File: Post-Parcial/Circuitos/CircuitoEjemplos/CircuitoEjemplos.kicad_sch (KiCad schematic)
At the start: 7 parts

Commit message: Cambio de estructura
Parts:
- removed J? (x2): Conn_01x19, symbol Connector_Generic:Conn_01x19
- added D3, D4: LED, symbol Device:LED
- added J1, J2: Conn_01x19, Connector_PinSocket_2.54mm:PinSocket_1x19_P2.54mm_Vertical, symbol Connector_Generic:Conn_01x19
- added R3, R4: 330, symbol Device:R
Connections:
- net GPIO4: now reaches R2.1
- net GPIO4: now also J2.13 (Pin_13)
- net at R2.2: now also D2.2 (A)
- net GND: now reaches D2.1 (K)
- net GND: now also D1.1 (K), D3.1 (K), D4.1 (K), J1.14 (Pin_14), J2.1 (Pin_1), J2.7 (Pin_7)
- net GPIO2: now reaches R1.1
- net GPIO2: now also J2.15 (Pin_15)
- net at R1.2: now also D1.2 (A)
- new net: D4.2 (A), R4.2
- new net: D3.2 (A), R3.2
- new net 3.3V: J1.1 (Pin_1)
- new net 5V: J1.19 (Pin_19)
- new net GPI34: J1.5 (Pin_5)
- new net GPI35: J1.6 (Pin_6)
- new net GPI36: J1.3 (Pin_3)
- new net GPI39: J1.4 (Pin_4)
- new net GPIO0: J2.14 (Pin_14)
- new net GPIO12: J1.13 (Pin_13)
- new net GPIO13: J1.15 (Pin_15)
- new net GPIO14: J1.12 (Pin_12)
- new net GPIO15: J2.16 (Pin_16)
- new net GPIO16: J2.12 (Pin_12), R3.1
- new net GPIO17: J2.11 (Pin_11), R4.1
- new net GPIO18: J2.9 (Pin_9)
- new net GPIO19: J2.8 (Pin_8)
- new net GPIO21: J2.6 (Pin_6)
- new net GPIO22: J2.3 (Pin_3)
- new net GPIO23: J2.2 (Pin_2)
- new net GPIO25: J1.9 (Pin_9)
- new net GPIO26: J1.10 (Pin_10)
- new net GPIO27: J1.11 (Pin_11)
- new net GPIO32: J1.7 (Pin_7)
- new net GPIO33: J1.8 (Pin_8)
- new net GPIO5: J2.10 (Pin_10)
- new net RX/GPIO3: J2.5 (Pin_5)
- new net TX/GPIO1: J2.4 (Pin_4)
- no-connect marks 0 -> 7
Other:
- note added: "Conexión de Led's"
- note added: "ESP32_Devkitc_V4"
- note added: "USB en este sentido"
- moved on the sheet: D1, R1, R2, RV1

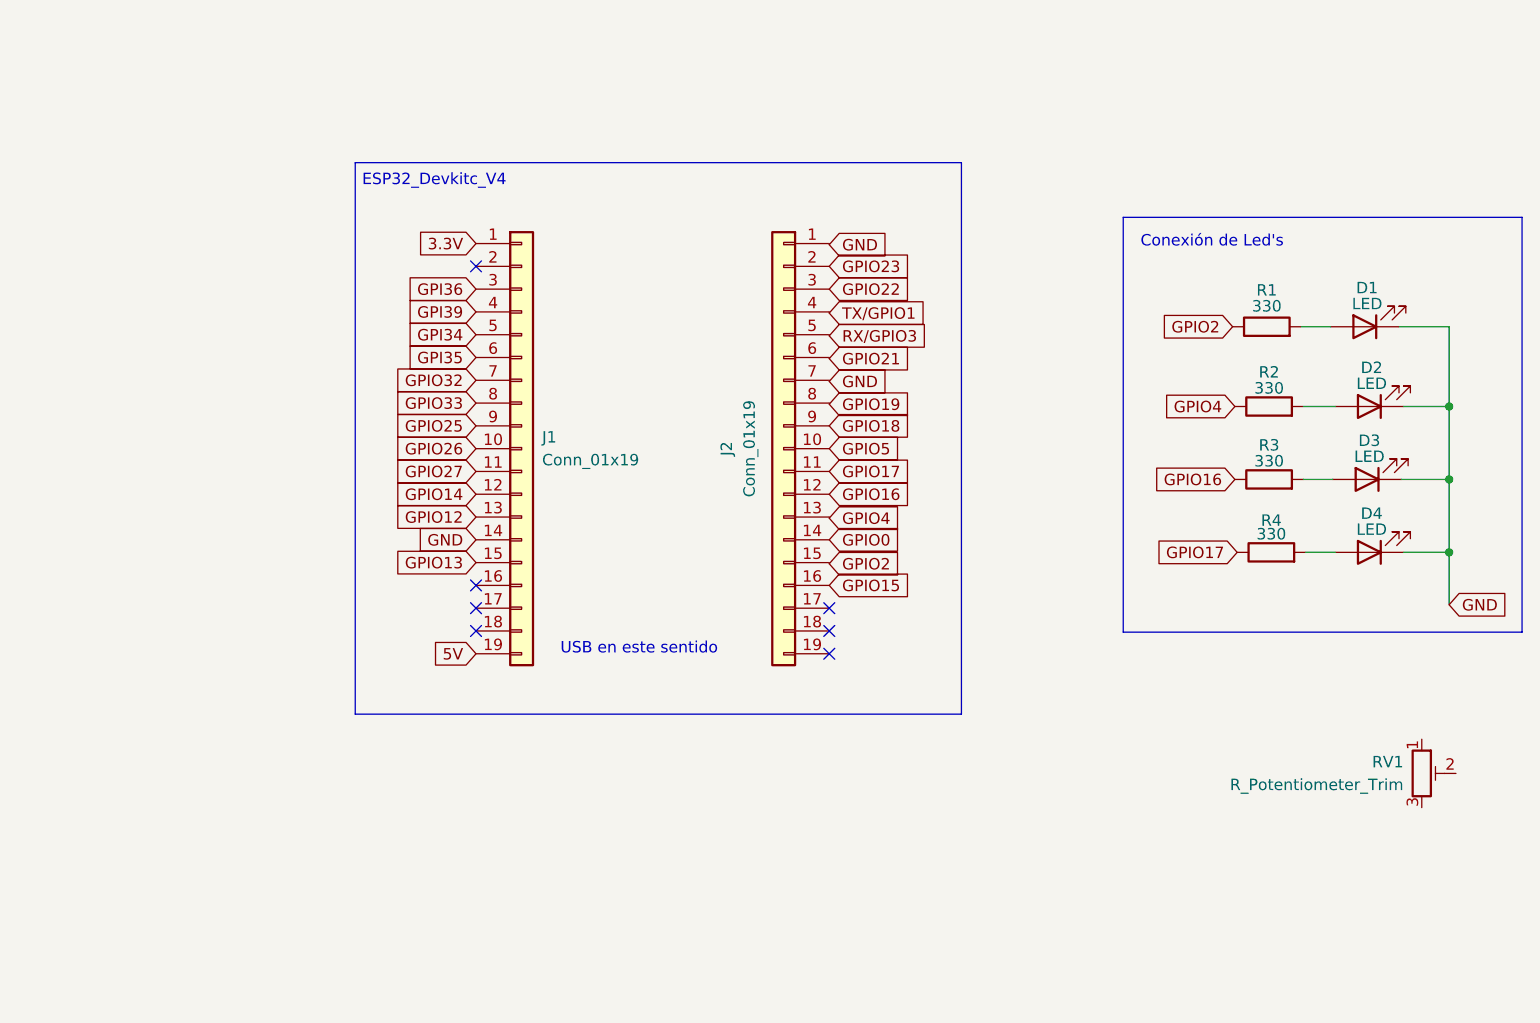
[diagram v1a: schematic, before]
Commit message: Avance en Circuito Ejemplos
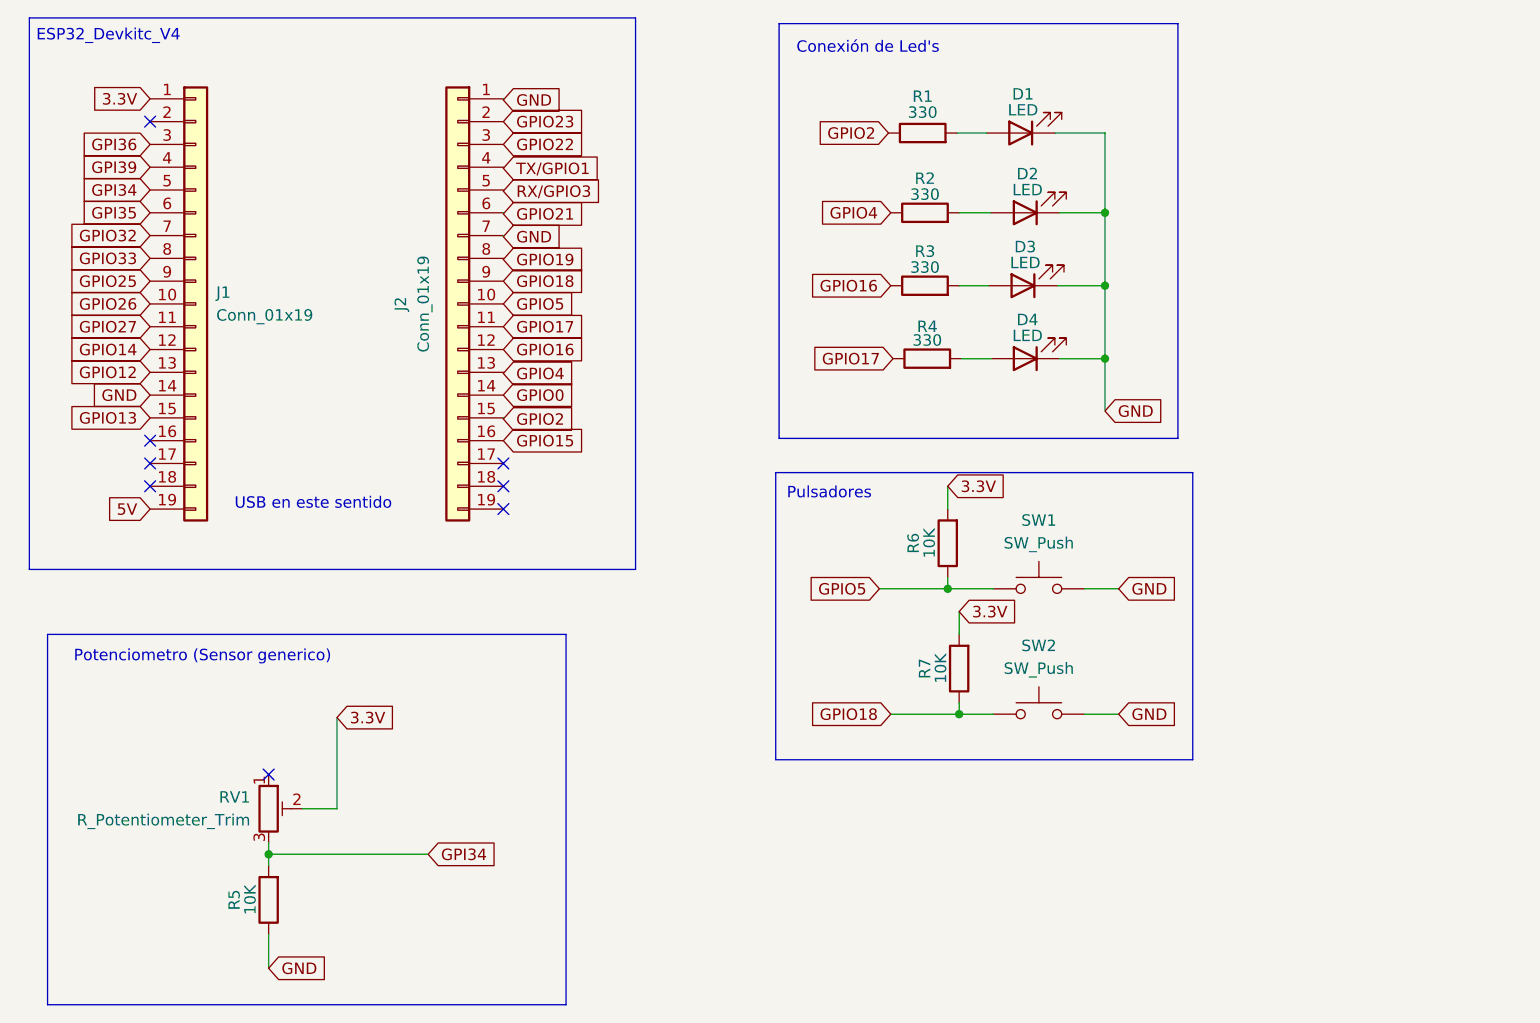
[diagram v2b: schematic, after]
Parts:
- added R5, R6, R7: 10K, symbol Device:R
- added SW1, SW2: SW_Push, symbol Switch:SW_Push
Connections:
- net 3.3V: now also RV1.2, R6.2, R7.2
- net GND: now also R5.1, SW1.2, SW2.2
- net GPI34: now also RV1.3, R5.2
- net GPIO18: now also R7.1, SW2.1
- net GPIO5: now also R6.1, SW1.1
- no-connect marks 7 -> 8
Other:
- note added: "Potenciometro (Sensor generico)"
- note added: "Pulsadores"
- moved on the sheet: D1, D2, D3, D4, J1, J2, R1, R2, R3, R4, RV1

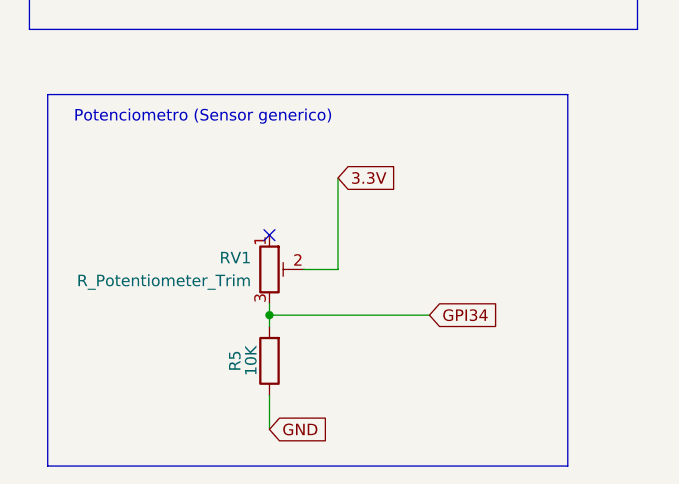
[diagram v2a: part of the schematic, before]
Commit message: Avance en directorio PostParcial
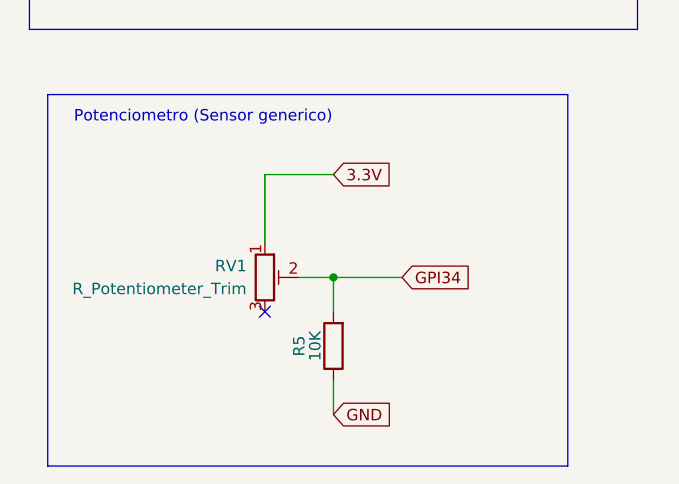
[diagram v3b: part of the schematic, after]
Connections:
- net 3.3V: now also RV1.1; no longer RV1.2
- net GPI34: now also RV1.2; no longer RV1.3
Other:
- moved on the sheet: R5, RV1
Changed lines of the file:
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@@
+	)
+	(junction
+		(at 104.14 129.54)
+		(diameter 0)
+		(color 0 0 0 0)
 	)
 	(junction
@@
 	)
 	(junction
-		(at 97.028 133.731)
-		(diameter 0)
-		(color 0 0 0 0)
-	)
-	(junction
 		(at 172.72 104.14)
 		(diameter 0)
@@
 	)
 	(no_connect
-		(at 97.028 124.841)
-	)
-	(no_connect
 		(at 123.19 92.71)
 	)
@@
 		(at 123.19 95.25)
 	)
+	(no_connect
+		(at 96.52 133.35)
+	)
+	(wire
+		(pts
+			(xy 96.52 118.11) (xy 96.52 125.73)
+		)
+		(stroke
+			(width 0)
+			(type default)
+		)
+	)
 	(wire
 		(pts
@@
 	(wire
 		(pts
+			(xy 104.14 118.11) (xy 96.52 118.11)
+		)
+		(stroke
+			(width 0)
+			(type default)
+		)
+	)
+	(wire
+		(pts
 			(xy 187.96 104.14) (xy 191.77 104.14)
 		)
@@
 	(wire
 		(pts
-			(xy 97.028 133.731) (xy 97.028 135.001)
-		)
-		(stroke
-			(width 0)
-			(type default)
-		)
-	)
-	(wire
-		(pts
 			(xy 123.19 59.69) (xy 123.19 59.817)
 		)
@@
 	(wire
 		(pts
-			(xy 97.028 132.461) (xy 97.028 133.731)
-		)
-		(stroke
-			(width 0)
-			(type default)
-		)
-	)
-	(wire
-		(pts
-			(xy 100.838 128.651) (xy 104.648 128.651)
-		)
-		(stroke
-			(width 0)
-			(type default)
-		)
-	)
-	(wire
-		(pts
 			(xy 174.244 78.486) (xy 177.546 78.486)
 		)
@@
 	(wire
 		(pts
-			(xy 97.028 142.621) (xy 97.028 146.431)
+			(xy 104.14 140.97) (xy 104.14 144.78)
 		)
 		(stroke
@@
 	(wire
 		(pts
-			(xy 114.808 133.731) (xy 97.028 133.731)
+			(xy 104.14 129.54) (xy 100.33 129.54)
 		)
 		(stroke
@@
 	(wire
 		(pts
+			(xy 104.14 129.54) (xy 111.76 129.54)
+		)
+		(stroke
+			(width 0)
+			(type default)
+		)
+	)
+	(wire
+		(pts
+			(xy 104.14 133.35) (xy 104.14 129.54)
+		)
+		(stroke
+			(width 0)
+			(type default)
+		)
+	)
+	(wire
+		(pts
 			(xy 172.72 102.87) (xy 172.72 104.14)
 		)
@@
 		(pts
 			(xy 190.246 62.23) (xy 190.246 70.358)
-		)
-		(stroke
-			(width 0)
-			(type default)
-		)
-	)
-	(wire
-		(pts
-			(xy 104.648 128.651) (xy 104.648 118.491)
 		)
 		(stroke
@@
 	(global_label "3.3V"
 		(shape input)
-		(at 104.648 118.491 0)
+		(at 104.14 118.11 0)
 		(fields_autoplaced yes)
 		(effects
@@
 		)
 		(property "Intersheetrefs" "${INTERSHEET_REFS}"
-			(at 111.7456 118.491 0)
+			(at 111.2376 118.11 0)
 			(effects
 				(font
@@
 	(global_label "GPI34"
 		(shape input)
-		(at 114.808 133.731 0)
+		(at 111.76 129.54 0)
 		(fields_autoplaced yes)
 		(effects
@@
 		)
 		(property "Intersheetrefs" "${INTERSHEET_REFS}"
-			(at 123.357 133.731 0)
+			(at 120.309 129.54 0)
 			(effects
 				(font
@@
 	(global_label "GND"
 		(shape input)
-		(at 97.028 146.431 0)
+		(at 104.14 144.78 0)
 		(fields_autoplaced yes)
 		(effects
@@
 		)
 		(property "Intersheetrefs" "${INTERSHEET_REFS}"
-			(at 103.8837 146.431 0)
+			(at 110.9957 144.78 0)
 			(effects
 				(font
@@
 	(symbol
 		(lib_id "Device:R_Potentiometer_Trim")
-		(at 97.028 128.651 0)
+		(at 96.52 129.54 0)
 		(unit 1)
 		(exclude_from_sim no)
@@
 		(fields_autoplaced yes)
 		(property "Reference" "RV1"
-			(at 94.996 127.3809 0)
+			(at 94.488 128.2699 0)
 			(effects
 				(font
@@
 		)
 		(property "Value" "R_Potentiometer_Trim"
-			(at 94.996 129.9209 0)
+			(at 94.488 130.8099 0)
 			(effects
 				(font
@@
 		)
 		(property "Footprint" ""
-			(at 97.028 128.651 0)
+			(at 96.52 129.54 0)
 			(effects
 				(font
@@
 		)
 		(property "Datasheet" "~"
-			(at 97.028 128.651 0)
+			(at 96.52 129.54 0)
 			(effects
 				(font
@@
 		)
 		(property "Description" "Trim-potentiometer"
-			(at 97.028 128.651 0)
+			(at 96.52 129.54 0)
 			(effects
 				(font
@@
 	(symbol
 		(lib_id "Device:R")
-		(at 97.028 138.811 180)
+		(at 104.14 137.16 180)
 		(unit 1)
 		(exclude_from_sim no)
@@
 		(dnp no)
 		(property "Reference" "R5"
-			(at 93.218 138.811 90)
+			(at 100.33 137.16 90)
 			(effects
 				(font
@@
 		)
 		(property "Value" "10K"
-			(at 94.996 138.811 90)
+			(at 102.108 137.16 90)
 			(effects
 				(font
@@
 		)
 		(property "Footprint" ""
-			(at 98.806 138.811 90)
+			(at 105.918 137.16 90)
 			(effects
 				(font
@@
 		)
 		(property "Datasheet" "~"
-			(at 97.028 138.811 0)
+			(at 104.14 137.16 0)
 			(effects
 				(font
@@
 		)
 		(property "Description" "Resistor"
-			(at 97.028 138.811 0)
-			(effects
-				(font
+			(at 104.14 137.16 0)
+			(effects
+				(font

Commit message: Ejemplos de Arduino Terminados
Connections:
- net 3.3V: now also R5.2; no longer RV1.1
- net GND: now also RV1.2; no longer R5.1
- net GPI34: no longer R5.2, RV1.2
- net GPI35: now also R5.1, RV1.1
- net GPIO18: no longer R7.1, SW2.1
- net GPIO32: now also R6.1, SW1.1
- net GPIO33: now also R7.1, SW2.1
- net GPIO5: no longer R6.1, SW1.1
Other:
- moved on the sheet: R5, RV1
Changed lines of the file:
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@@
-	)
-	(junction
-		(at 104.14 129.54)
-		(diameter 0)
-		(color 0 0 0 0)
 	)
 	(junction
@@
 	)
 	(junction
+		(at 99.314 129.794)
+		(diameter 0)
+		(color 0 0 0 0)
+	)
+	(junction
 		(at 172.72 104.14)
 		(diameter 0)
@@
 	)
 	(no_connect
-		(at 96.52 133.35)
-	)
-	(wire
-		(pts
-			(xy 96.52 118.11) (xy 96.52 125.73)
-		)
-		(stroke
-			(width 0)
-			(type default)
-		)
+		(at 99.314 139.954)
 	)
 	(wire
@@
 	(wire
 		(pts
+			(xy 103.124 136.144) (xy 109.474 136.144)
+		)
+		(stroke
+			(width 0)
+			(type default)
+		)
+	)
+	(wire
+		(pts
 			(xy 184.912 70.358) (xy 190.246 70.358)
 		)
@@
 	(wire
 		(pts
-			(xy 104.14 118.11) (xy 96.52 118.11)
+			(xy 106.934 116.586) (xy 99.314 116.586)
 		)
 		(stroke
@@
 	(wire
 		(pts
+			(xy 99.314 116.586) (xy 99.314 119.634)
+		)
+		(stroke
+			(width 0)
+			(type default)
+		)
+	)
+	(wire
+		(pts
 			(xy 165.1 104.14) (xy 172.72 104.14)
 		)
@@
 	(wire
 		(pts
+			(xy 99.314 129.794) (xy 99.314 132.334)
+		)
+		(stroke
+			(width 0)
+			(type default)
+		)
+	)
+	(wire
+		(pts
 			(xy 123.19 64.77) (xy 123.19 64.897)
 		)
@@
 	(wire
 		(pts
+			(xy 99.314 127.254) (xy 99.314 129.794)
+		)
+		(stroke
+			(width 0)
+			(type default)
+		)
+	)
+	(wire
+		(pts
 			(xy 185.166 62.23) (xy 190.246 62.23)
 		)
@@
 	(wire
 		(pts
-			(xy 104.14 140.97) (xy 104.14 144.78)
-		)
-		(stroke
-			(width 0)
-			(type default)
-		)
-	)
-	(wire
-		(pts
 			(xy 190.246 84.328) (xy 190.246 78.486)
 		)
@@
 	(wire
 		(pts
-			(xy 104.14 129.54) (xy 100.33 129.54)
-		)
-		(stroke
-			(width 0)
-			(type default)
-		)
-	)
-	(wire
-		(pts
 			(xy 123.19 85.09) (xy 123.19 85.217)
 		)
@@
 	(wire
 		(pts
-			(xy 104.14 129.54) (xy 111.76 129.54)
-		)
-		(stroke
-			(width 0)
-			(type default)
-		)
-	)
-	(wire
-		(pts
-			(xy 104.14 133.35) (xy 104.14 129.54)
+			(xy 99.314 129.794) (xy 114.554 129.794)
 		)
 		(stroke
@@
 	(global_label "3.3V"
 		(shape input)
-		(at 104.14 118.11 0)
+		(at 106.934 116.586 0)
 		(fields_autoplaced yes)
 		(effects
@@
 		)
 		(property "Intersheetrefs" "${INTERSHEET_REFS}"
-			(at 111.2376 118.11 0)
+			(at 114.0316 116.586 0)
 			(effects
 				(font
@@
 		)
 	)
-	(global_label "GPIO18"
+	(global_label "GPIO33"
 		(shape input)
 		(at 166.37 118.11 180)
@@
 		)
 	)
-	(global_label "GPIO5"
+	(global_label "GPIO32"
 		(shape input)
 		(at 165.1 104.14 180)
@@
 		)
 		(property "Intersheetrefs" "${INTERSHEET_REFS}"
-			(at 156.43 104.14 0)
+			(at 155.2205 104.14 0)
 			(effects
 				(font
@@
 		)
 	)
-	(global_label "GPI34"
-		(shape input)
-		(at 111.76 129.54 0)
+	(global_label "GPI35"
+		(shape input)
+		(at 114.554 129.794 0)
 		(fields_autoplaced yes)
 		(effects
@@
 		)
 		(property "Intersheetrefs" "${INTERSHEET_REFS}"
-			(at 120.309 129.54 0)
+			(at 123.103 129.794 0)
 			(effects
 				(font
@@
 	(global_label "GND"
 		(shape input)
-		(at 104.14 144.78 0)
+		(at 109.474 136.144 0)
 		(fields_autoplaced yes)
 		(effects
@@
 		)
 		(property "Intersheetrefs" "${INTERSHEET_REFS}"
-			(at 110.9957 144.78 0)
+			(at 116.3297 136.144 0)
 			(effects
 				(font
@@
 	(symbol
 		(lib_id "Device:R_Potentiometer_Trim")
-		(at 96.52 129.54 0)
+		(at 99.314 136.144 0)
 		(unit 1)
 		(exclude_from_sim no)
@@
 		(fields_autoplaced yes)
 		(property "Reference" "RV1"
-			(at 94.488 128.2699 0)
+			(at 97.282 134.8739 0)
 			(effects
 				(font
@@
 		)
 		(property "Value" "R_Potentiometer_Trim"
-			(at 94.488 130.8099 0)
+			(at 97.282 137.4139 0)
 			(effects
 				(font
@@
 		)
 		(property "Footprint" ""
-			(at 96.52 129.54 0)
+			(at 99.314 136.144 0)
 			(effects
 				(font
@@
 		)
 		(property "Datasheet" "~"
-			(at 96.52 129.54 0)
+			(at 99.314 136.144 0)
 			(effects
 				(font
@@
 		)
 		(property "Description" "Trim-potentiometer"
-			(at 96.52 129.54 0)
+			(at 99.314 136.144 0)
 			(effects
 				(font
@@
 	(symbol
 		(lib_id "Device:R")
-		(at 104.14 137.16 180)
+		(at 99.314 123.444 180)
 		(unit 1)
 		(exclude_from_sim no)
@@
 		(dnp no)
 		(property "Reference" "R5"
-			(at 100.33 137.16 90)
+			(at 95.504 123.444 90)
 			(effects
 				(font
@@
 		)
 		(property "Value" "10K"
-			(at 102.108 137.16 90)
+			(at 97.282 123.444 90)
 			(effects
 				(font
@@
 		)
 		(property "Footprint" ""
-			(at 105.918 137.16 90)
+			(at 101.092 123.444 90)
 			(effects
 				(font
@@
 		)
 		(property "Datasheet" "~"
-			(at 104.14 137.16 0)
+			(at 99.314 123.444 0)
 			(effects
 				(font
@@
 		)
 		(property "Description" "Resistor"
-			(at 104.14 137.16 0)
-			(effects
-				(font
+			(at 99.314 123.444 0)
+			(effects
+				(font
